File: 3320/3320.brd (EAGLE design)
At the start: 57.8 x 216.2 mm, 69 parts, among them IC1 OPA2134P, IC2 OPA2134P, X1 2516-

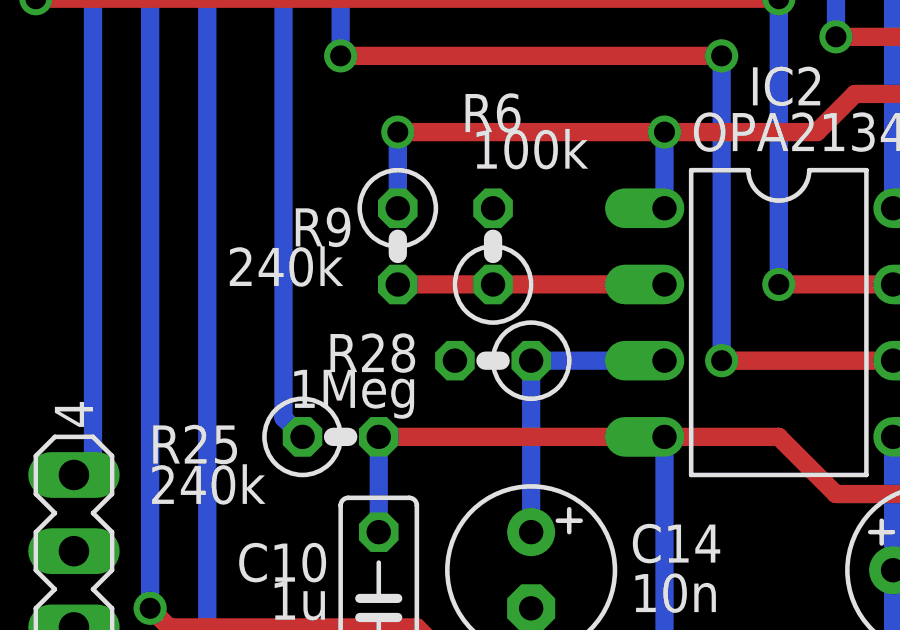
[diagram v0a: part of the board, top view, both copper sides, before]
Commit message: fixed the 2 pole polarity for 3320
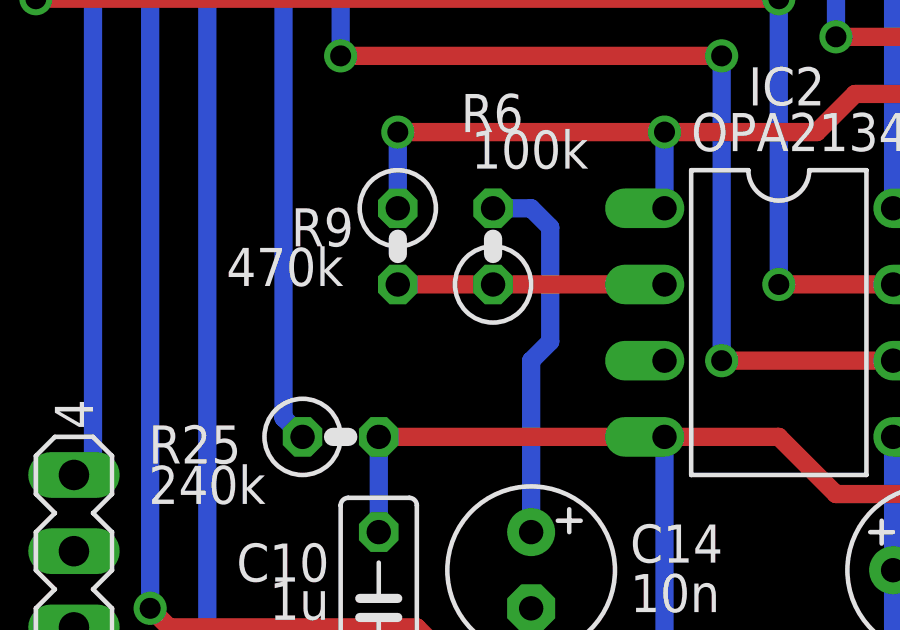
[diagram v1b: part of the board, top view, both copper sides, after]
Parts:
- removed R28: 1Meg, dan:0207/2V
- R9: value 240k -> 470k
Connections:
- net GND: now also IC2.3; no longer R28.2, R6.2
- net N$11: now also R6.2; no longer IC2.3, R28.1
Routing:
- net N$11: track 10.2 -> 12.6 mm
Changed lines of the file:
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@@
 <attribute name="VALUE" x="33.7058" y="163.83" size="1.27" layer="21" font="vector" ratio="15" rot="R90"/>
 </element>
-<element name="R9" library="dan" package="0207/2V" value="240k" x="15.24" y="20.32" smashed="yes" rot="R270">
+<element name="R9" library="dan" package="0207/2V" value="470k" x="15.24" y="20.32" smashed="yes" rot="R270">
 <attribute name="NAME" x="11.684" y="20.32" size="1.27" layer="21" font="vector" ratio="15"/>
 <attribute name="VALUE" x="9.525" y="18.9992" size="1.27" layer="21" font="vector" ratio="15"/>
@@
 <attribute name="NAME" x="22.987" y="9.779" size="1.27" layer="21" font="vector" ratio="15"/>
 <attribute name="VALUE" x="22.987" y="8.128" size="1.27" layer="21" font="vector" ratio="15"/>
-</element>
-<element name="R28" library="dan" package="0207/2V" value="1Meg" x="18.415" y="16.51" smashed="yes" rot="R180">
-<attribute name="NAME" x="15.9258" y="17.399" size="1.27" layer="21" font="vector" ratio="15" rot="R180"/>
-<attribute name="VALUE" x="15.9258" y="16.2052" size="1.27" layer="21" font="vector" ratio="15" rot="R180"/>
 </element>
 <element name="C15" library="dan" package="E2,5-6" value="2.2u" x="37.465" y="76.2" smashed="yes" rot="R90">
@@
 <contactref element="SV3" pad="2"/>
 <contactref element="SV3" pad="3"/>
-<contactref element="R6" pad="2"/>
 <contactref element="R13" pad="2"/>
 <polygon width="0.4064" layer="1">
@@
 <contactref element="U$1" pad="3"/>
 <contactref element="R23" pad="1"/>
-<contactref element="R28" pad="2"/>
 <contactref element="C15" pad="-"/>
 <contactref element="C16" pad="+"/>
@@
 <contactref element="D3" pad="C"/>
 <contactref element="Q" pad="1"/>
+<contactref element="IC2" pad="3"/>
 <wire x1="4.445" y1="113.03" x2="4.445" y2="100.33" width="0" layer="19" extent="1-1"/>
 </signal>
@@
 </signal>
 <signal name="N$11">
-<contactref element="IC2" pad="3"/>
 <contactref element="C14" pad="+"/>
-<contactref element="R28" pad="1"/>
-<wire x1="24.13" y1="16.51" x2="19.685" y2="16.51" width="0.6096" layer="16"/>
+<contactref element="R6" pad="2"/>
 <wire x1="19.685" y1="10.795" x2="19.685" y2="16.51" width="0.6096" layer="16"/>
+<wire x1="19.685" y1="16.51" x2="20.32" y2="17.145" width="0.6096" layer="16"/>
+<wire x1="20.32" y1="17.145" x2="20.32" y2="20.955" width="0.6096" layer="16"/>
+<wire x1="20.32" y1="20.955" x2="19.685" y2="21.59" width="0.6096" layer="16"/>
+<wire x1="19.685" y1="21.59" x2="18.415" y2="21.59" width="0.6096" layer="16"/>
 </signal>
 <signal name="N$13">

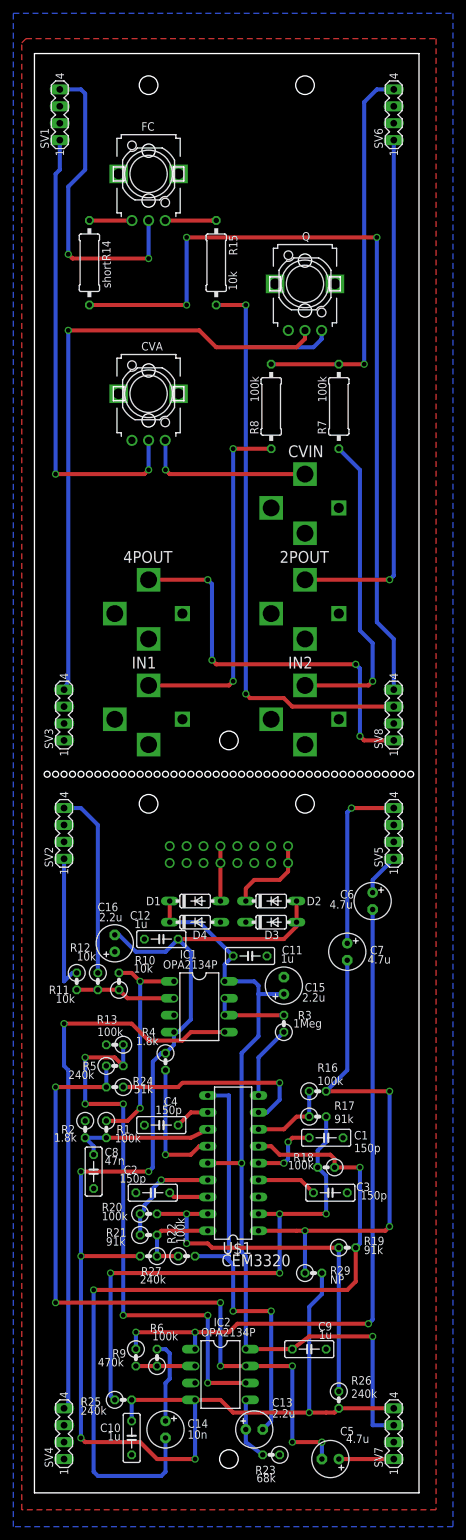
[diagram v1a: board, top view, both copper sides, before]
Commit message: fixed footprints on top 3320 board
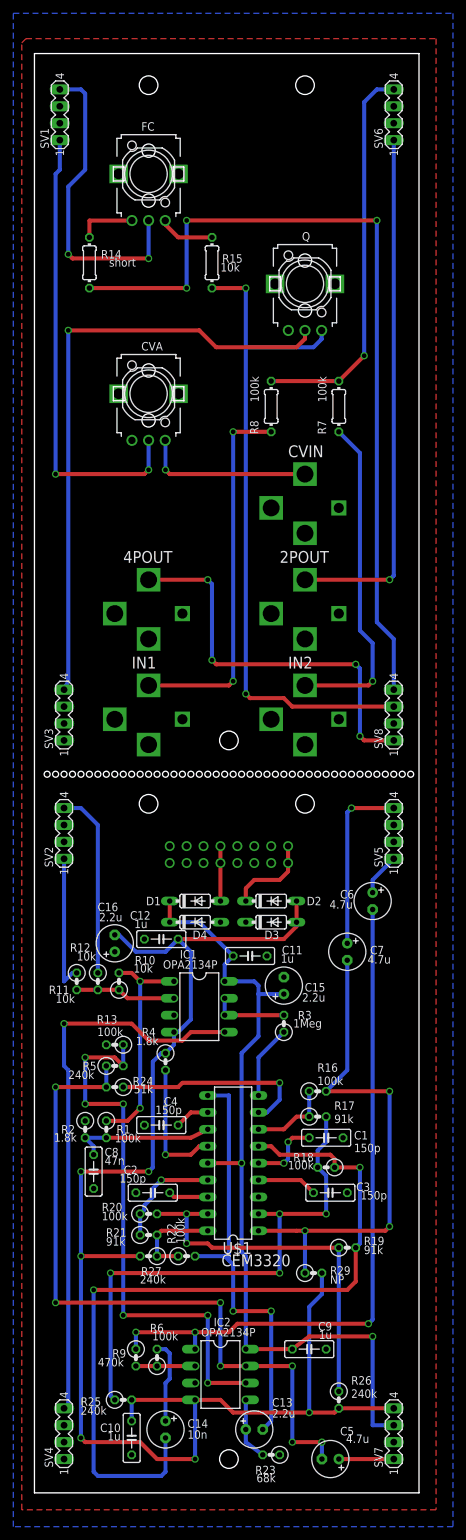
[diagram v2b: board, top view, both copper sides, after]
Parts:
- R14, R15, R7, R8: device dan:0309/12 -> dan:0204/7
- moved R15 0.63 mm to (26.7, 184.8)
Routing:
- net +12V: track 224.6 -> 227.7 mm
- net N$29: track 47.5 -> 50.0 mm
- net N$15: track 53.6 -> 56.1 mm
- net -12V: track 346.9 -> 349.5 mm
- net N$6: track 6.40 -> 8.90 mm
- net N$7: track 7.66 -> 8.41 mm
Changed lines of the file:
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@@
 <attribute name="VALUE" x="13.335" y="69.9008" size="1.27" layer="21" font="vector" ratio="15" rot="R180"/>
 </element>
-<element name="R14" library="dan" package="0309/12" value="short" x="8.255" y="184.785" smashed="yes" rot="R90">
-<attribute name="NAME" x="11.43" y="185.039" size="1.27" layer="21" font="vector" ratio="15" rot="R90"/>
-<attribute name="VALUE" x="11.4808" y="180.975" size="1.27" layer="21" font="vector" ratio="15" rot="R90"/>
-</element>
-<element name="R15" library="dan" package="0309/12" value="10k" x="27.305" y="184.785" smashed="yes" rot="R270">
-<attribute name="NAME" x="29.21" y="188.976" size="1.27" layer="21" font="vector" ratio="15" rot="R270"/>
-<attribute name="VALUE" x="29.1592" y="183.515" size="1.27" layer="21" font="vector" ratio="15" rot="R270"/>
+<element name="R14" library="dan" package="0204/7" value="short" x="8.255" y="184.785" smashed="yes" rot="R90">
+<attribute name="NAME" x="13.081" y="186.69" size="1.27" layer="21" font="vector" ratio="15" rot="R180"/>
+<attribute name="VALUE" x="15.24" y="185.4708" size="1.27" layer="21" font="vector" ratio="15" rot="R180"/>
+</element>
+<element name="R15" library="dan" package="0204/7" value="10k" x="26.67" y="184.785" smashed="yes" rot="R270">
+<attribute name="NAME" x="28.194" y="184.785" size="1.27" layer="21" font="vector" ratio="15"/>
+<attribute name="VALUE" x="27.94" y="183.4642" size="1.27" layer="21" font="vector" ratio="15"/>
 </element>
 <element name="R2" library="dan" package="0207/2V" value="1.8k" x="7.62" y="54.61" smashed="yes" rot="R270">
@@
 <attribute name="VALUE" x="21.59" y="24.1808" size="1.27" layer="21" font="vector" ratio="15" rot="R180"/>
 </element>
-<element name="R7" library="dan" package="0309/12" value="100k" x="45.72" y="163.195" smashed="yes" rot="R90">
+<element name="R7" library="dan" package="0204/7" value="100k" x="45.72" y="163.195" smashed="yes" rot="R90">
 <attribute name="NAME" x="43.815" y="159.004" size="1.27" layer="21" font="vector" ratio="15" rot="R90"/>
 <attribute name="VALUE" x="43.8658" y="163.83" size="1.27" layer="21" font="vector" ratio="15" rot="R90"/>
 </element>
-<element name="R8" library="dan" package="0309/12" value="100k" x="35.56" y="163.195" smashed="yes" rot="R90">
+<element name="R8" library="dan" package="0204/7" value="100k" x="35.56" y="163.195" smashed="yes" rot="R90">
 <attribute name="NAME" x="33.655" y="159.004" size="1.27" layer="21" font="vector" ratio="15" rot="R90"/>
 <attribute name="VALUE" x="33.7058" y="163.83" size="1.27" layer="21" font="vector" ratio="15" rot="R90"/>
@@
 <contactref element="C11" pad="1"/>
 <contactref element="IC2" pad="8"/>
-<wire x1="27.305" y1="178.435" x2="31.75" y2="178.435" width="0.6096" layer="1"/>
+<wire x1="26.67" y1="180.975" x2="31.75" y2="180.975" width="0.6096" layer="1"/>
 <wire x1="53.975" y1="118.11" x2="38.735" y2="118.11" width="0.6096" layer="1"/>
 <wire x1="38.735" y1="118.11" x2="37.465" y2="119.38" width="0.6096" layer="1"/>
@@
 <via x="31.75" y="120.015" extent="1-16" drill="0.7"/>
 <wire x1="31.75" y1="120.015" x2="31.75" y2="172.085" width="0.6096" layer="16"/>
-<via x="31.75" y="178.435" extent="1-16" drill="0.7"/>
-<wire x1="31.75" y1="172.085" x2="31.75" y2="178.435" width="0.6096" layer="16"/>
+<via x="31.75" y="180.975" extent="1-16" drill="0.7"/>
+<wire x1="31.75" y1="172.085" x2="31.75" y2="180.975" width="0.6096" layer="16"/>
 <contactref element="U$1" pad="14"/>
 <wire x1="38.735" y1="21.59" x2="31.75" y2="21.59" width="0.6096" layer="1"/>
@@
 <wire x1="53.975" y1="120.65" x2="53.975" y2="128.27" width="0.6096" layer="16"/>
 <wire x1="53.975" y1="128.27" x2="51.435" y2="130.81" width="0.6096" layer="16"/>
-<wire x1="51.435" y1="130.81" x2="51.435" y2="188.595" width="0.6096" layer="16"/>
-<via x="51.435" y="188.595" extent="1-16" drill="0.7"/>
-<wire x1="51.435" y1="188.595" x2="22.86" y2="188.595" width="0.6096" layer="1"/>
-<wire x1="22.86" y1="188.595" x2="22.86" y2="178.435" width="0.6096" layer="16"/>
-<wire x1="22.86" y1="178.435" x2="8.255" y2="178.435" width="0.6096" layer="1"/>
-<via x="22.86" y="188.595" extent="1-16" drill="0.7"/>
-<via x="22.86" y="178.435" extent="1-16" drill="0.7"/>
+<wire x1="51.435" y1="130.81" x2="51.435" y2="191.135" width="0.6096" layer="16"/>
+<via x="51.435" y="191.135" extent="1-16" drill="0.7"/>
+<wire x1="22.86" y1="191.135" x2="22.86" y2="180.975" width="0.6096" layer="16"/>
+<wire x1="22.86" y1="180.975" x2="8.255" y2="180.975" width="0.6096" layer="1"/>
+<via x="22.86" y="191.135" extent="1-16" drill="0.7"/>
+<via x="22.86" y="180.975" extent="1-16" drill="0.7"/>
 <contactref element="R27" pad="2"/>
 <contactref element="R26" pad="2"/>
@@
 <wire x1="23.495" y1="81.28" x2="21.59" y2="83.185" width="0.6096" layer="16"/>
 <wire x1="29.845" y1="12.065" x2="41.275" y2="12.065" width="0.6096" layer="1"/>
-<wire x1="43.815" y1="12.065" x2="45.085" y2="12.065" width="0.6096" layer="1"/>
 <wire x1="45.085" y1="12.065" x2="45.72" y2="12.7" width="0.6096" layer="1"/>
 <wire x1="24.13" y1="13.97" x2="24.13" y2="5.08" width="0.6096" layer="16"/>
@@
 <wire x1="41.275" y1="27.94" x2="41.275" y2="12.065" width="0.6096" layer="16"/>
 <via x="41.275" y="12.065" extent="1-16" drill="0.7"/>
-<wire x1="41.275" y1="12.065" x2="43.815" y2="12.065" width="0.6096" layer="1"/>
+<wire x1="41.275" y1="12.065" x2="45.085" y2="12.065" width="0.6096" layer="1"/>
+<wire x1="22.86" y1="191.135" x2="51.435" y2="191.135" width="0.6096" layer="1"/>
 <wire x1="39.37" y1="88.9" x2="53.975" y2="120.65" width="0" layer="19" extent="1-1"/>
 </signal>
@@
 <contactref element="FC" pad="1"/>
 <wire x1="14.645" y1="191.12" x2="8.27" y2="191.12" width="0.6096" layer="1"/>
-<wire x1="8.27" y1="191.12" x2="8.255" y2="191.135" width="0.6096" layer="1"/>
+<wire x1="8.27" y1="191.12" x2="8.255" y2="188.595" width="0.6096" layer="1"/>
 </signal>
 <signal name="N$7">
 <contactref element="FC" pad="3"/>
 <contactref element="R15" pad="1"/>
-<wire x1="19.645" y1="191.12" x2="26.655" y2="191.12" width="0.6096" layer="1"/>
-<wire x1="26.655" y1="191.12" x2="27.305" y2="191.135" width="0.6096" layer="1"/>
+<wire x1="26.67" y1="188.595" x2="21.59" y2="188.595" width="0.6096" layer="1"/>
+<wire x1="21.59" y1="188.595" x2="19.685" y2="190.5" width="0.6096" layer="1"/>
+<wire x1="19.685" y1="190.5" x2="19.685" y2="191.08" width="0.6096" layer="1"/>
+<wire x1="19.685" y1="191.08" x2="19.645" y2="191.12" width="0.6096" layer="1"/>
 </signal>
 <signal name="N$5">
@@
 <wire x1="29.21" y1="121.285" x2="29.845" y2="121.92" width="0.6096" layer="1"/>
 <via x="29.845" y="121.92" extent="1-16" drill="0.7"/>
-<wire x1="29.845" y1="121.92" x2="29.845" y2="156.845" width="0.6096" layer="16"/>
-<via x="29.845" y="156.845" extent="1-16" drill="0.7"/>
-<wire x1="29.845" y1="156.845" x2="35.56" y2="156.845" width="0.6096" layer="1"/>
+<wire x1="29.845" y1="121.92" x2="29.845" y2="159.385" width="0.6096" layer="16"/>
+<via x="29.845" y="159.385" extent="1-16" drill="0.7"/>
+<wire x1="29.845" y1="159.385" x2="35.56" y2="159.385" width="0.6096" layer="1"/>
 </signal>
 <signal name="N$27">
@@
 <contactref element="SV6" pad="4"/>
 <contactref element="R7" pad="2"/>
-<wire x1="35.56" y1="169.545" x2="45.72" y2="169.545" width="0.6096" layer="1"/>
+<wire x1="35.56" y1="167.005" x2="45.72" y2="167.005" width="0.6096" layer="1"/>
 <wire x1="53.975" y1="210.82" x2="51.435" y2="210.82" width="0.6096" layer="16"/>
 <wire x1="51.435" y1="210.82" x2="49.53" y2="208.915" width="0.6096" layer="16"/>
-<wire x1="49.53" y1="208.915" x2="49.53" y2="169.545" width="0.6096" layer="16"/>
-<via x="49.53" y="169.545" extent="1-16" drill="0.7"/>
-<wire x1="49.53" y1="169.545" x2="45.72" y2="169.545" width="0.6096" layer="1"/>
+<wire x1="49.53" y1="208.915" x2="49.53" y2="170.815" width="0.6096" layer="16"/>
+<via x="49.53" y="170.815" extent="1-16" drill="0.7"/>
+<wire x1="49.53" y1="170.815" x2="45.72" y2="167.005" width="0.6096" layer="1"/>
 </signal>
 <signal name="N$29">
@@
 <wire x1="50.8" y1="121.92" x2="50.8" y2="127.635" width="0.6096" layer="16"/>
 <wire x1="50.8" y1="127.635" x2="48.895" y2="129.54" width="0.6096" layer="16"/>
-<wire x1="48.895" y1="129.54" x2="48.895" y2="153.67" width="0.6096" layer="16"/>
-<wire x1="48.895" y1="153.67" x2="45.72" y2="156.845" width="0.6096" layer="16"/>
+<wire x1="48.895" y1="129.54" x2="48.895" y2="156.21" width="0.6096" layer="16"/>
+<wire x1="48.895" y1="156.21" x2="45.72" y2="159.385" width="0.6096" layer="16"/>
 </signal>
 <signal name="N$12">

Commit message: added input atten pots to 3320 and re arranged front
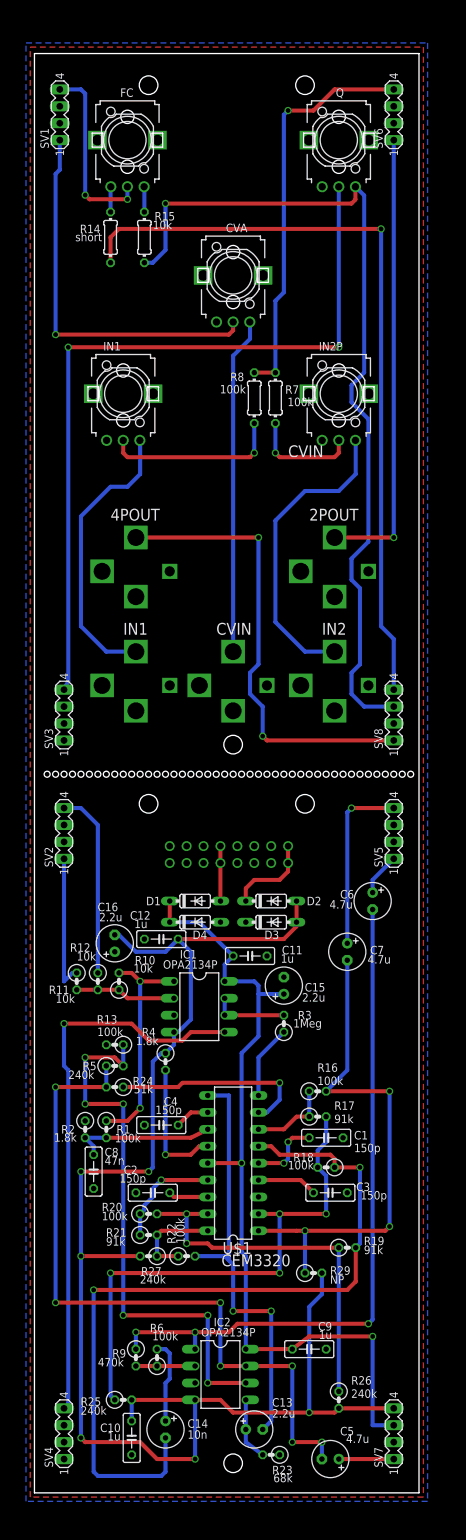
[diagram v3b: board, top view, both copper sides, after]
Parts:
- added IN1, IN2P: US-EVUF2J, dan:EVUFXJ
- moved CVIN 28.8 mm to (29.8, 121.3)
- moved Q 22.2 mm to (45.7, 203.2)
- moved CVA 21.8 mm to (29.8, 182.9)
- moved R15 10.9 mm to (16.5, 188.6)
- moved R7 9.61 mm to (36.2, 164.5)
- moved 2POUT 7.75 mm to (45.1, 138.4)
- moved IN2 6.75 mm to (45.1, 121.3)
- moved 4POUTPUT 6.63 mm to (15.2, 138.4)
- moved FC 5.99 mm to (14.0, 203.2)
- moved IN 5.43 mm to (15.2, 121.3)
- moved R14 4.96 mm to (11.4, 188.6)
- moved R8 2.84 mm to (33.0, 164.5)
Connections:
- new net N$44: IN.P$3, IN1.3
- new net N$46: IN2.P$3, IN2P.3
- net GND: now also IN1.1, IN2P.1
- net N$15: now also IN1.2; no longer IN.P$3
- net N$29: now also IN2P.2; no longer IN2.P$3
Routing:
- net N$46: track 0.00 -> 46.0 mm
- net N$44: track 0.00 -> 42.9 mm
- net N$29: track 50.0 -> 16.4 mm
- net N$15: track 56.1 -> 26.5 mm, vias 2 -> 1
- net +12V: track 227.7 -> 255.0 mm, vias 4 -> 3
- net N$22: track 25.7 -> 50.6 mm, vias 1 -> 0
- net N$23: track 92.5 -> 116.3 mm, vias 1 -> 2
- net N$5: track 47.3 -> 27.8 mm
- net N$31: track 69.1 -> 57.7 mm, vias 2 -> 1
- net N$26: track 79.0 -> 68.6 mm
- net N$32: track 59.5 -> 69.5 mm, vias 4 -> 2
- net -12V: track 349.5 -> 339.6 mm, vias 9 -> 7
- net N$6: track 8.90 -> 3.81 mm
- net N$7: track 8.41 -> 3.81 mm
- net N$27: track 58.9 -> 60.5 mm
